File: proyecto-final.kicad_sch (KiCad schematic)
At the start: 2 parts, among them U1 AD797, U2 74AHC273

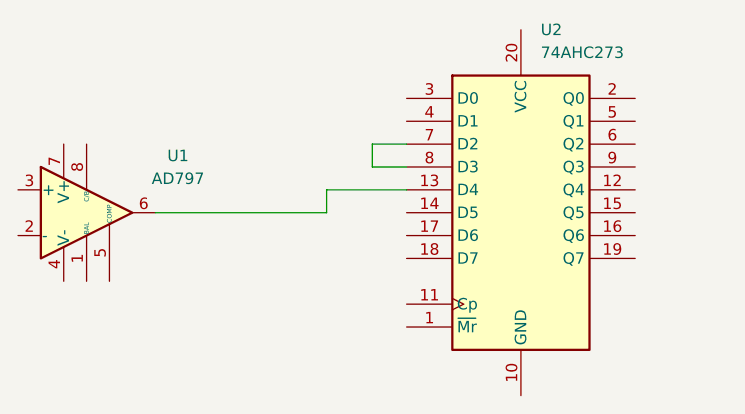
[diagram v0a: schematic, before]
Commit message: Modifique la ruta xxx
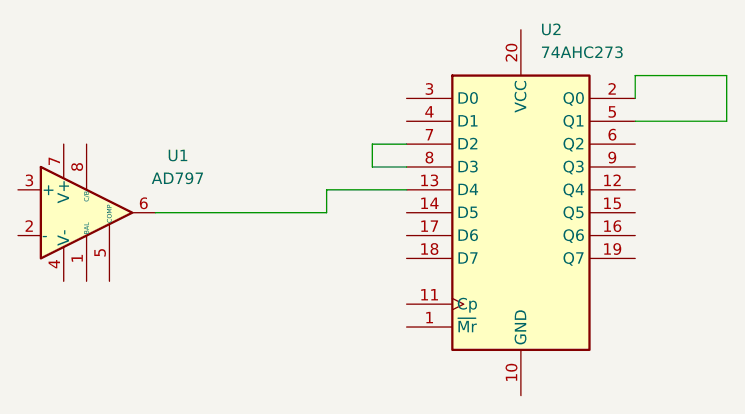
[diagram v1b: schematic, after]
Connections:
- net at U2.2 (Q0): now also U2.5 (Q1)
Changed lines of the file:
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@@
+	(wire
+		(pts
+			(xy 152.4 60.96) (xy 162.56 60.96)
+		)
+		(stroke
+			(width 0)
+			(type default)
+		)
+	)
 	(wire
 		(pts
@@
 	(wire
 		(pts
+			(xy 162.56 55.88) (xy 152.4 55.88)
+		)
+		(stroke
+			(width 0)
+			(type default)
+		)
+	)
+	(wire
+		(pts
+			(xy 162.56 60.96) (xy 162.56 55.88)
+		)
+		(stroke
+			(width 0)
+			(type default)
+		)
+	)
+	(wire
+		(pts
 			(xy 99.06 71.12) (xy 118.11 71.12)
 		)
 		(stroke
+			(width 0)
+			(type default)
+		)
+	)
+	(wire
+		(pts
+			(xy 152.4 55.88) (xy 152.4 58.42)
+		)
+		(stroke
